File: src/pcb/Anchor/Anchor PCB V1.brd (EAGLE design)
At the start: 100.1 x 68.7 mm, 88 parts, among them IC1 ENC28J60-I_SS, IC2 TPS23750PWP, IC3 MIC5219-3.3YM5-TR, IC4 DWM1000, J1 0826-1X1T-GJ-F, J2 105017-0001, Q1 32 MHz, Q2 SUD06N10-225L, U1 ATSAMD21G-A, Y1 25 MHz

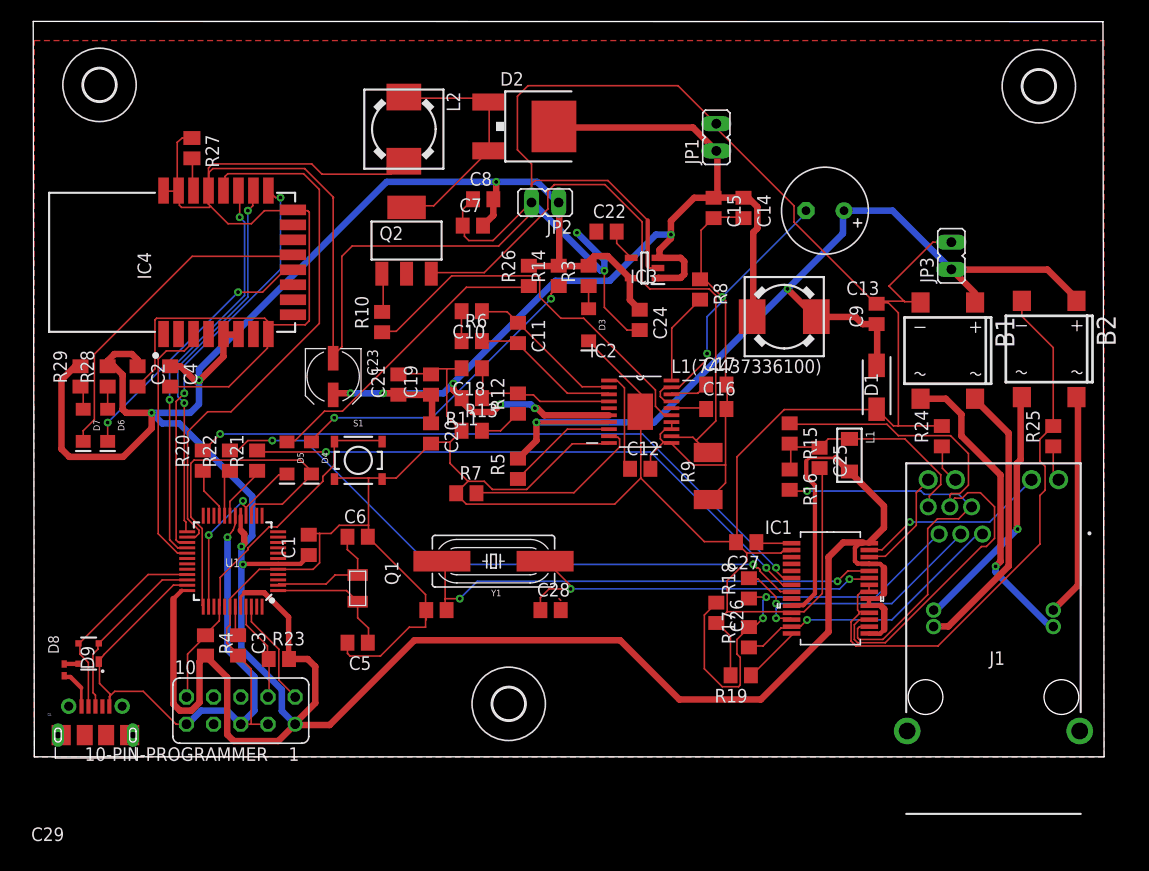
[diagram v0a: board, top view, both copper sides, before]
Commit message: Bugfixes wiring
Added PCB files
Bugfixes
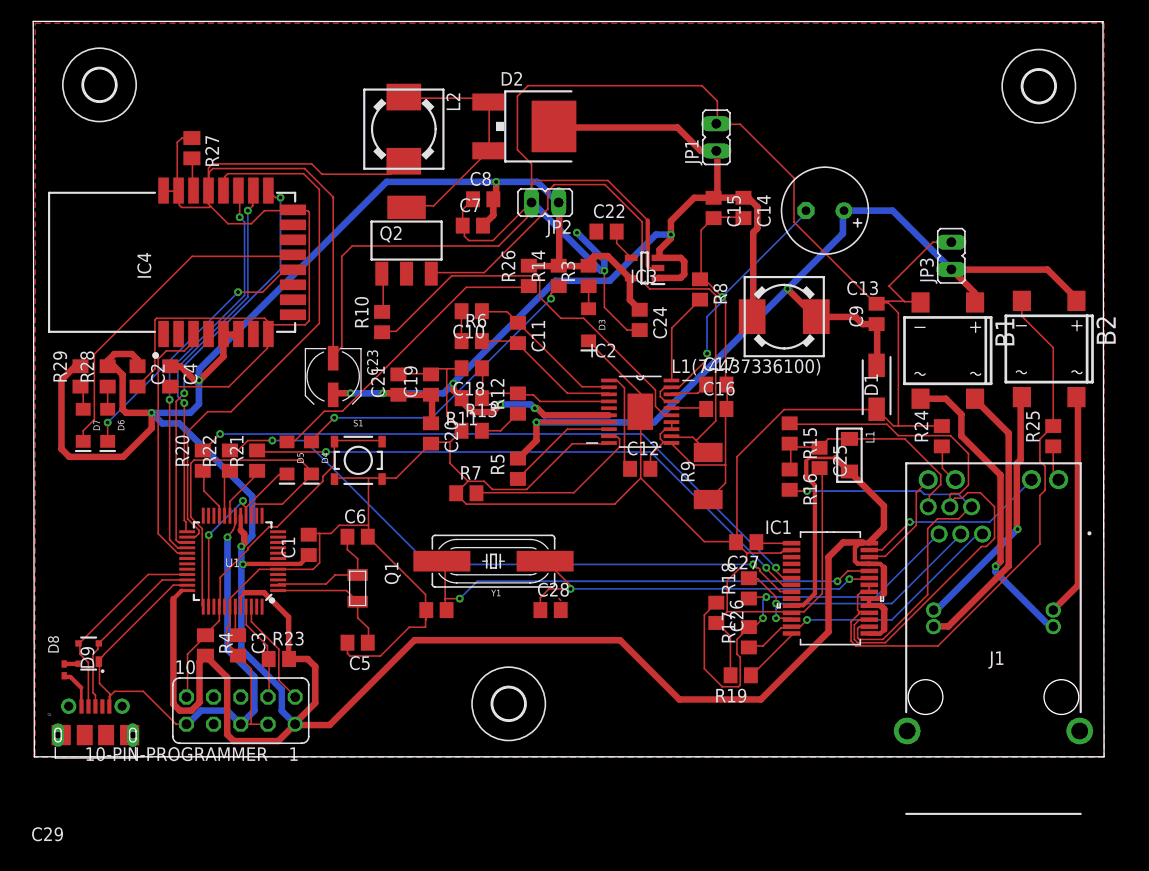
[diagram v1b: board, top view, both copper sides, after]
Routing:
- net GND: track 617.7 -> 620.3 mm
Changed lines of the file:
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@@
 <layers>
 <layer number="1" name="Top" color="4" fill="1" visible="yes" active="yes"/>
+<layer number="2" name="Route2" color="16" fill="1" visible="no" active="yes"/>
+<layer number="3" name="Route3" color="17" fill="1" visible="no" active="yes"/>
+<layer number="4" name="Route4" color="18" fill="1" visible="no" active="yes"/>
+<layer number="5" name="Route5" color="19" fill="1" visible="no" active="yes"/>
+<layer number="6" name="Route6" color="25" fill="1" visible="no" active="yes"/>
+<layer number="7" name="Route7" color="26" fill="1" visible="no" active="yes"/>
+<layer number="8" name="Route8" color="27" fill="1" visible="no" active="yes"/>
+<layer number="9" name="Route9" color="28" fill="1" visible="no" active="yes"/>
+<layer number="10" name="Route10" color="29" fill="1" visible="no" active="yes"/>
+<layer number="11" name="Route11" color="30" fill="1" visible="no" active="yes"/>
+<layer number="12" name="Route12" color="20" fill="1" visible="no" active="yes"/>
+<layer number="13" name="Route13" color="21" fill="1" visible="no" active="yes"/>
+<layer number="14" name="Route14" color="22" fill="1" visible="no" active="yes"/>
+<layer number="15" name="Route15" color="23" fill="1" visible="no" active="yes"/>
 <layer number="16" name="Bottom" color="1" fill="1" visible="yes" active="yes"/>
 <layer number="17" name="Pads" color="2" fill="1" visible="yes" active="yes"/>
@@
 <wire x1="99.8984" y1="68.7224" x2="-0.1016" y2="68.7478" width="0" layer="20"/>
 <wire x1="-0.1016" y1="68.7478" x2="0" y2="0" width="0" layer="20"/>
-<dimension x1="100" y1="0" x2="99.8984" y2="68.7224" x3="111.78028125" y3="34.378690625" textsize="1.778" layer="1"/>
-<dimension x1="-0.1016" y1="68.7478" x2="99.8984" y2="68.7224" x3="49.89881875" y3="70.39534375" textsize="1.778" layer="1"/>
 </plain>
 <attributes>
@@
 </class>
 </classes>
-<designrules name="default">
+<designrules name="default *">
 <description language="de">&lt;b&gt;EAGLE Design Rules&lt;/b&gt;
 &lt;p&gt;
@@
 <param name="mdViaViaSameLayer" value="6mil"/>
 <param name="mnLayersViaInSmd" value="2"/>
-<param name="mdCopperDimension" value="40mil"/>
+<param name="mdCopperDimension" value="0mil"/>
 <param name="mdDrill" value="6mil"/>
 <param name="mdSmdStop" value="0mil"/>
@@
 <wire x1="78.6384" y1="32.4612" x2="78.74" y2="32.494" width="0.1524" layer="1"/>
 <wire x1="65.6844" y1="20.1168" x2="65.598" y2="20.066" width="0.1524" layer="1"/>
-<wire x1="63.8556" y1="58.674" x2="63.8556" y2="59.055" width="0.1524" layer="1"/>
+<wire x1="65.9892" y1="59.1312" x2="63.8556" y2="59.1312" width="0.1524" layer="1"/>
+<wire x1="63.8556" y1="59.1312" x2="63.8556" y2="61.2902" width="0.1524" layer="1"/>
 <wire x1="63.8556" y1="59.055" x2="63.8556" y2="59.1312" width="0.1524" layer="1"/>
-<wire x1="71.0184" y1="51.5112" x2="63.8556" y2="58.674" width="0.1524" layer="1"/>
-<wire x1="71.0184" y1="49.9872" x2="71.0184" y2="51.5112" width="0.1524" layer="1"/>
+<wire x1="71.0184" y1="54.102" x2="65.9892" y2="59.1312" width="0.1524" layer="1"/>
+<wire x1="71.0184" y1="49.9872" x2="71.0184" y2="54.102" width="0.1524" layer="1"/>
 <wire x1="78.6384" y1="42.3672" x2="71.0184" y2="49.9872" width="0.1524" layer="1"/>
 <wire x1="63.8556" y1="59.1312" x2="63.754" y2="59.182" width="0.1524" layer="1"/>
@@
 <wire x1="94.488" y1="27.1526" x2="94.0054" y2="27.6352" width="0.1524" layer="1"/>
 <polygon width="0.4064" layer="1">
-<vertex x="0" y="0.0762"/>
-<vertex x="0" y="66.9544"/>
-<vertex x="99.9744" y="66.9544"/>
-<vertex x="99.9998" y="66.9798"/>
+<vertex x="0.0795875" y="0.1557875"/>
+<vertex x="0.0795875" y="68.58"/>
+<vertex x="99.9998" y="68.58"/>
 <vertex x="99.9998" y="-0.0254"/>
 <vertex x="0.0254" y="-0.0254"/>
@@
 <wire x1="45.1612" y1="56.7436" x2="45.1612" y2="61.7474" width="0.1524" layer="1"/>
 <wire x1="45.1612" y1="61.7474" x2="46.1518" y2="62.738" width="0.1524" layer="1"/>
-<wire x1="60.1726" y1="62.738" x2="63.8556" y2="59.055" width="0.1524" layer="1"/>
-<wire x1="46.1518" y1="62.738" x2="60.1726" y2="62.738" width="0.1524" layer="1"/>
+<wire x1="62.4078" y1="62.738" x2="63.8556" y2="61.2902" width="0.1524" layer="1"/>
+<wire x1="46.1518" y1="62.738" x2="62.4078" y2="62.738" width="0.1524" layer="1"/>
 <wire x1="56.5912" y1="39.8932" x2="55.4076" y2="39.8932" width="0.1524" layer="1"/>
 <wire x1="55.4076" y1="39.8932" x2="53.2892" y2="42.0116" width="0.1524" layer="1"/>
@@
 <wire x1="67.2084" y1="41.148" x2="67.104" y2="41.148" width="0.6096" layer="1"/>
 <wire x1="63.5" y1="52.258" x2="61.6814" y2="52.258" width="0.6096" layer="1"/>
-<wire x1="61.5696" y1="58.8264" x2="48.6156" y2="58.8264" width="0.6096" layer="1"/>
-<wire x1="63.754" y1="56.642" x2="61.5696" y2="58.8264" width="0.6096" layer="1"/>
+<wire x1="60.1218" y1="58.8264" x2="48.6156" y2="58.8264" width="0.6096" layer="1"/>
+<wire x1="63.754" y1="56.642" x2="62.3062" y2="56.642" width="0.6096" layer="1"/>
+<wire x1="62.3062" y1="56.642" x2="60.1218" y2="58.8264" width="0.6096" layer="1"/>
 <wire x1="48.6156" y1="58.8264" x2="48.578" y2="58.928" width="0.6096" layer="1"/>
 <wire x1="48.7172" y1="44.5008" x2="39.1668" y2="34.9504" width="0.6096" layer="16"/>

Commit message: Final version
Thicker traces where possible
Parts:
- moved R7 8.68 mm to (49.0, 25.2), turned to 90 degrees
- moved R18 2.99 mm to (63.8, 15.6)
- moved C26 2.28 mm to (63.8, 11.2)
- moved D6 0.44 mm to (6.41, 31.0)
- moved R29 0.42 mm to (3.90, 35.6)
- moved D7 0.41 mm to (4.17, 31.0)
- moved R28 0.29 mm to (6.57, 35.5)
- moved C2 0.24 mm to (9.41, 35.6)
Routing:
- net GND: track 620.3 -> 42.0 mm, vias 3 -> 7
- net TPOUT+: track 52.7 -> 39.9 mm
- net N$6: track 40.8 -> 30.6 mm
- net N$3: track 17.0 -> 7.26 mm
- net TPIN-: track 26.7 -> 30.1 mm
- net N$12: track 28.7 -> 31.9 mm
- net RTN: track 69.4 -> 71.9 mm
- net VCC: track 330.5 -> 332.6 mm
- net 2_VC-: track 26.4 -> 28.2 mm
- net MOSI2_MC: track 35.3 -> 37.0 mm
- net 1_VC-: track 24.1 -> 25.7 mm
- net 2_VC+: track 28.4 -> 29.9 mm
- net 48V: track 92.1 -> 93.2 mm
- net RST_DWM: track 24.5 -> 25.5 mm
- net 5V: track 113.3 -> 114.2 mm
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- added copper zone on layer 16, net GND

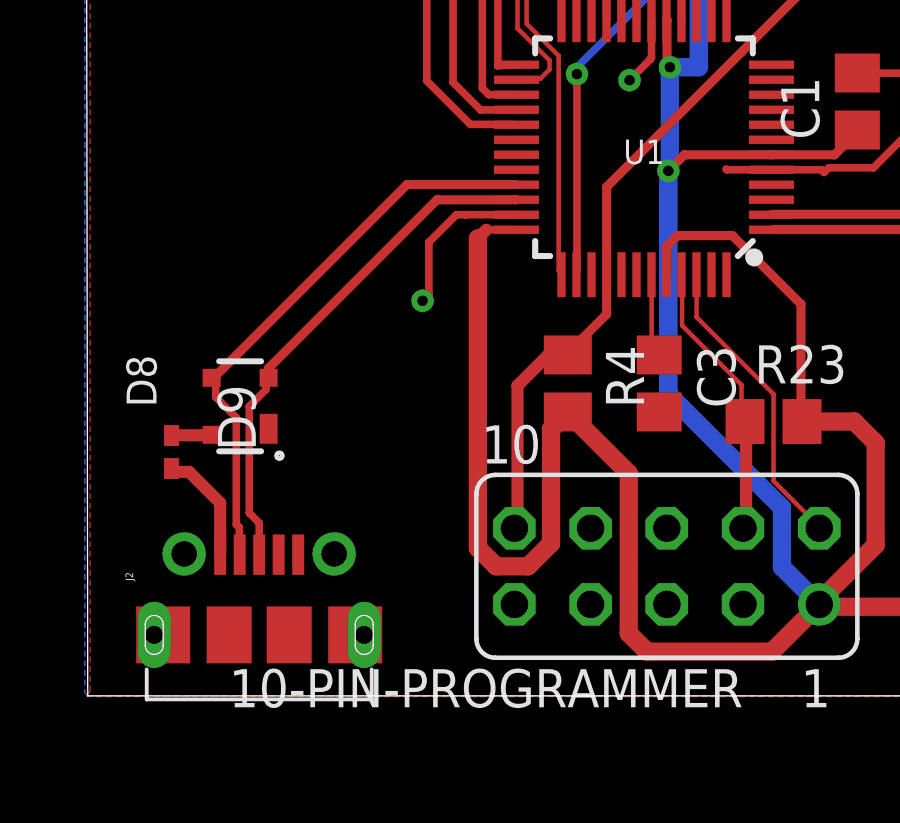
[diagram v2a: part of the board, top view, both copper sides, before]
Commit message: Added jumper for TX and RX of MCU
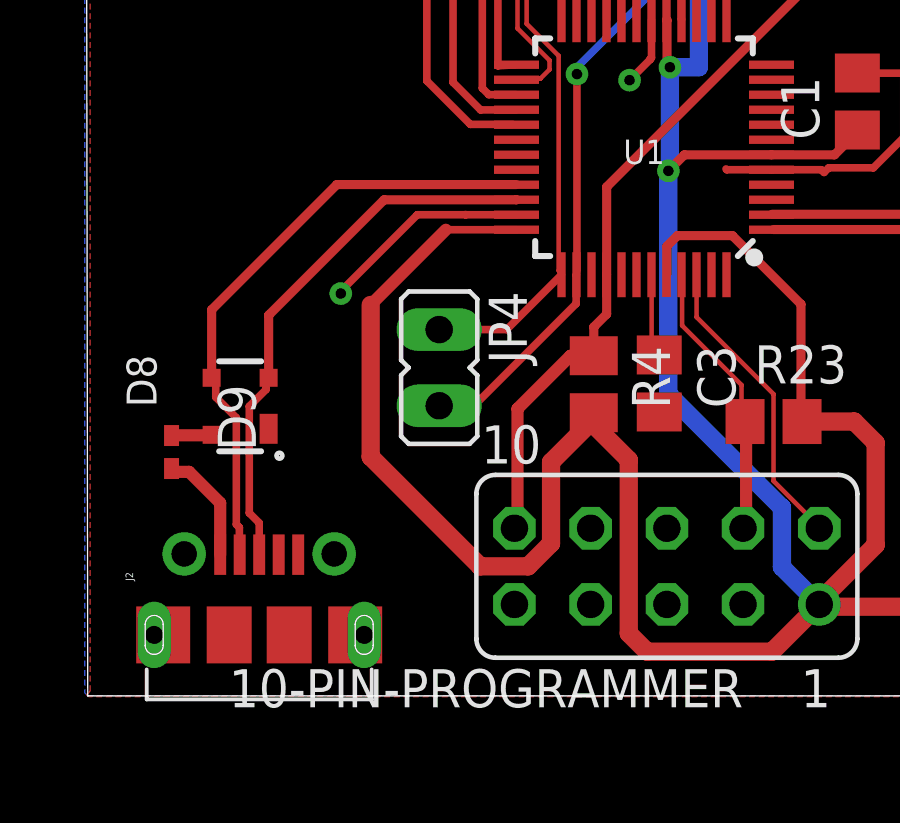
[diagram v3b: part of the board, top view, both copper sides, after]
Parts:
- added JP4: (no value), jumper:JP1
- moved R4 0.87 mm to (16.9, 10.4)
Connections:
- net RX_MC: now also JP4.2
- net TX_MC: now also JP4.1
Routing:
- net RX_MC: track 18.7 -> 25.7 mm
- net TX_MC: track 34.8 -> 39.6 mm
- net VCC: track 332.6 -> 336.6 mm
- net GND: track 42.0 -> 43.6 mm
- net USB-: track 19.3 -> 20.7 mm
- net USB+: track 17.2 -> 18.2 mm

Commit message: Changed footprint 33µH
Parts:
- L2: device inductors:DR73 -> wurth_elektronik_passive_rev16d:WE-PD_1260/1245/1280/1210
- moved L2 3.73 mm to (32.1, 61.5), turned to 180 degrees
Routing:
- net COM_A_SHTKY: track 22.6 -> 20.1 mm
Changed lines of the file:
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@@
 <attribute name="VALUE" x="35.052" y="40.005" size="1.27" layer="27" rot="R90"/>
 </element>
-<element name="L2" library="inductors" library_urn="urn:adsk.eagle:library:243" package="DR73" package3d_urn="urn:adsk.eagle:package:15123/1" value="33 µH" x="34.544" y="58.674" smashed="yes" rot="R270">
-<attribute name="NAME" x="38.544" y="62.174" size="1.27" layer="25" rot="R270"/>
-<attribute name="SPICEPREFIX" value="L" x="34.544" y="58.674" size="1.778" layer="27" rot="R270" display="off"/>
-<attribute name="VALUE" x="29.044" y="62.174" size="1.27" layer="27" rot="R270"/>
+<element name="L2" library="wurth_elektronik_passive_rev16d" package="WE-PD_1260/1245/1280/1210" value="33 µH" x="32.10051875" y="61.48831875" smashed="yes" rot="R180">
+<attribute name="NAME" x="35.60051875" y="57.48831875" size="1.27" layer="25" rot="R180"/>
+<attribute name="VALUE" x="35.60051875" y="66.98831875" size="1.27" layer="27" rot="R180"/>
 </element>
 <element name="D2" library="shottky" package="DPAK" package3d_urn="urn:adsk.eagle:package:28765/1" value="6CWQ10FN" x="46.482" y="58.928" smashed="yes" rot="R270">
@@
 <wire x1="42.5196" y1="56.6928" x2="42.442" y2="56.648" width="0.1524" layer="1"/>
 <wire x1="42.5196" y1="61.1124" x2="42.442" y2="61.208" width="0.1524" layer="1"/>
-<wire x1="42.0624" y1="61.5696" x2="34.5948" y2="61.5696" width="0.6096" layer="1"/>
-<wire x1="42.3672" y1="61.2648" x2="42.0624" y2="61.5696" width="0.1524" layer="1"/>
-<wire x1="34.5948" y1="61.5696" x2="34.544" y2="61.674" width="0.1524" layer="1"/>
-<wire x1="42.3672" y1="61.2648" x2="42.442" y2="61.208" width="0.1524" layer="1"/>
+<wire x1="42.442" y1="61.208" x2="42.34131875" y2="61.10731875" width="0.6096" layer="1"/>
+<wire x1="42.34131875" y1="61.10731875" x2="42.01368125" y2="61.10731875" width="0.6096" layer="1"/>
+<wire x1="42.01368125" y1="61.10731875" x2="41.940021875" y2="61.180978125" width="0.6096" layer="1"/>
+<wire x1="41.940021875" y1="61.180978125" x2="37.357859375" y2="61.180978125" width="0.6096" layer="1"/>
+<wire x1="37.357859375" y1="61.180978125" x2="37.05051875" y2="61.48831875" width="0.6096" layer="1"/>
 <wire x1="37.338" y1="51.5112" x2="34.8996" y2="51.5112" width="0.6096" layer="1"/>
 <wire x1="42.3672" y1="56.5404" x2="37.338" y2="51.5112" width="0.6096" layer="1"/>

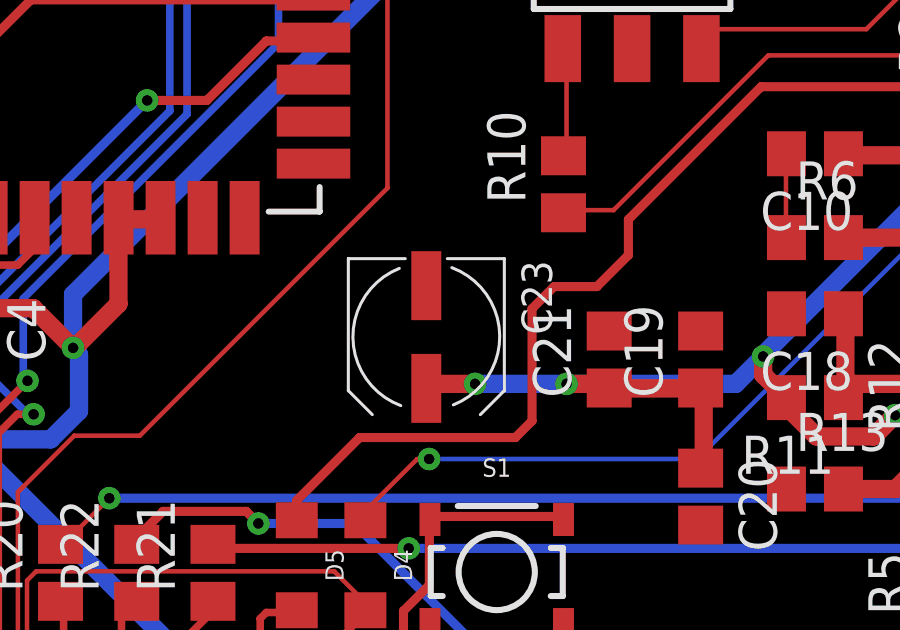
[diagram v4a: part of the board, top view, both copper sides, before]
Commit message: Update anchor wrong footprints
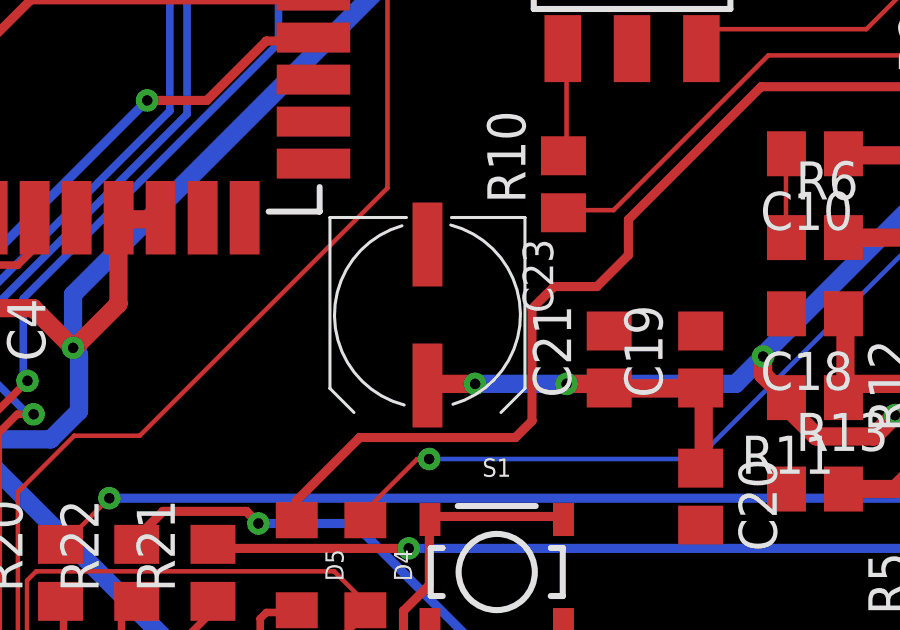
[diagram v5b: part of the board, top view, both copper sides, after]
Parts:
- C23: device rcl:UD-5X5,8_NICHICON -> rcl:UD-6,3X7,7_NICHICON
- moved C23 0.72 mm to (28.0, 36.3)
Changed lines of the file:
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@@
 <attribute name="VALUE" x="36.576" y="33.528" size="1.27" layer="27" rot="R90"/>
 </element>
-<element name="C23" library="rcl" library_urn="urn:adsk.eagle:library:334" package="UD-5X5,8_NICHICON" package3d_urn="urn:adsk.eagle:package:23470/1" value="100 µF (6.3V)" x="27.94" y="35.56" smashed="yes" rot="R270">
-<attribute name="NAME" x="31.115" y="38.1" size="1.016" layer="25" rot="R270"/>
-<attribute name="SPICEPREFIX" value="C" x="27.94" y="35.56" size="1.778" layer="27" rot="R270" display="off"/>
-<attribute name="VALUE" x="24.13" y="38.1" size="1.016" layer="27" rot="R270"/>
+<element name="C23" library="rcl" library_urn="urn:adsk.eagle:library:334" package="UD-6,3X7,7_NICHICON" package3d_urn="urn:adsk.eagle:package:23472/1" value="100 µF (6.3V)" x="27.978103125" y="36.281359375" smashed="yes" rot="R270">
+<attribute name="NAME" x="31.153103125" y="38.821359375" size="1.016" layer="25" rot="R270"/>
+<attribute name="SPICEPREFIX" value="C" x="27.978103125" y="36.281359375" size="1.778" layer="27" rot="R270" display="off"/>
+<attribute name="VALUE" x="24.168103125" y="38.821359375" size="1.016" layer="27" rot="R270"/>
 </element>
 <element name="JP1" library="jumper" library_urn="urn:adsk.eagle:library:252" package="JP1" package3d_urn="urn:adsk.eagle:package:15455/1" value="" x="63.754" y="57.912" smashed="yes">
@@
 <contactref element="JP3" pad="2"/>
 <wire x1="46.482" y1="51.816" x2="46.5836" y2="51.816" width="0.1524" layer="16"/>
-<wire x1="27.94" y1="37.5158" x2="27.94" y2="37.26" width="0.1524" layer="1"/>
+<wire x1="27.978103125" y1="38.237159375" x2="27.978103125" y2="38.631359375" width="0.1524" layer="1"/>
 <wire x1="21.7932" y1="39.624" x2="21.884" y2="39.523" width="0.1524" layer="1"/>
 <wire x1="12.8016" y1="34.5948" x2="12.7" y2="34.61" width="0.1524" layer="1"/>
@@
 <wire x1="37.1856" y1="31.242" x2="37.084" y2="31.176" width="0.6096" layer="1"/>
 <wire x1="37.1856" y1="33.8328" x2="37.084" y2="33.848" width="0.6096" layer="1"/>
-<wire x1="29.5656" y1="33.9852" x2="28.0416" y2="33.9852" width="0.6096" layer="1"/>
+<wire x1="29.5656" y1="33.9852" x2="27.985159375" y2="33.9852" width="0.6096" layer="1"/>
 <wire x1="32.6136" y1="33.9852" x2="29.5656" y2="33.9852" width="0.6096" layer="16"/>
 <wire x1="33.9852" y1="33.9852" x2="32.6136" y2="33.9852" width="0.6096" layer="1"/>
-<wire x1="28.0416" y1="33.9852" x2="27.94" y2="33.835" width="0.6096" layer="1"/>
+<wire x1="27.985159375" y1="33.9852" x2="27.978103125" y2="33.931359375" width="0.6096" layer="1"/>
 <wire x1="33.9852" y1="33.9852" x2="34.036" y2="33.848" width="0.6096" layer="1"/>
 <wire x1="42.8498" y1="32.2326" x2="43.561" y2="32.9438" width="0.6096" layer="1"/>
